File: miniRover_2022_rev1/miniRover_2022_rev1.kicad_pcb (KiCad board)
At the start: 2 copper layers, 11 parts, among them J1 XT60-M, U1 OKI, U2 DRV8871-Breakout-PCB, U3 DRV8871-Breakout-PCB, U4 DRV8871-Breakout-PCB, U5 DRV8871-Breakout-PCB, U6 DRV8871-Breakout-PCB, U7 DRV8871-Breakout-PCB

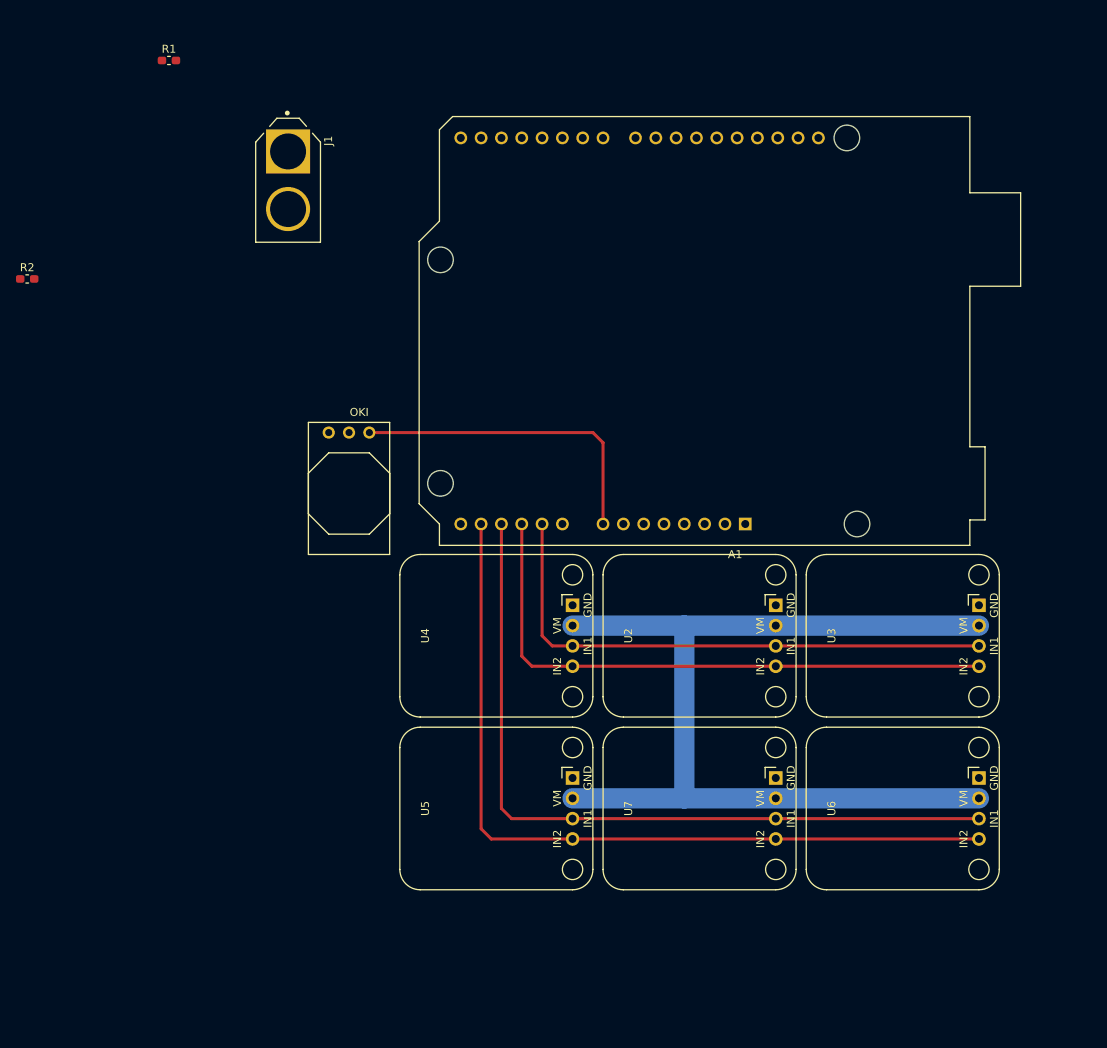
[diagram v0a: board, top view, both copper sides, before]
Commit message: gnd planes added
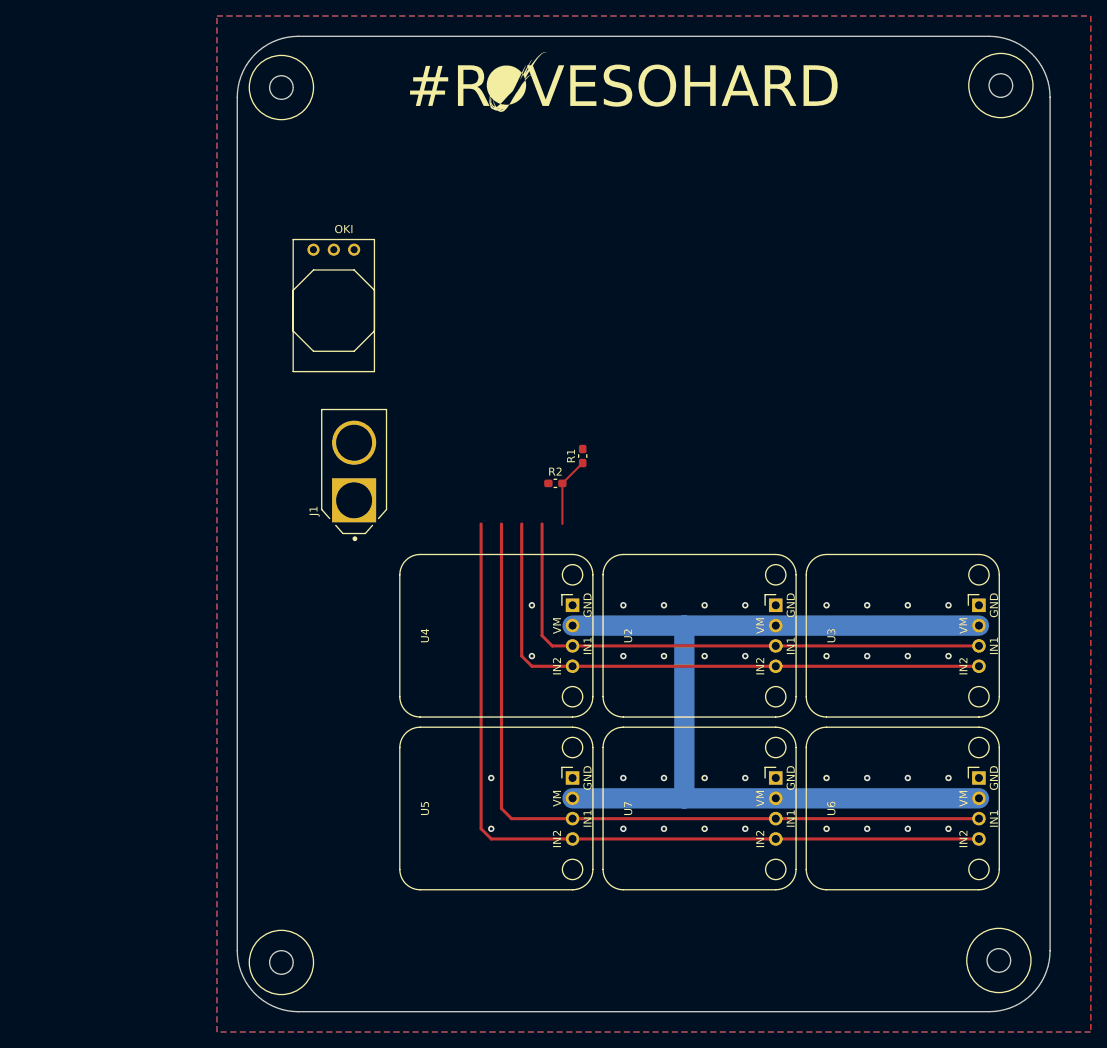
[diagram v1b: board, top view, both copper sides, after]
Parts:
- removed A1: Arduino_UNO_R3, Module:Arduino_UNO_R3_WithMountingHoles
- added G***: LOGO, MRDT_Silkscreens:0_MRDT_Logo_7.5mm, F.Cu at (149.2, 21.0)
- added REF**: 4_40_Hole, MRDT_Drill_Holes:4_40_Hole_Corner, F.Cu at (205.5, 126.8)
- added REF**: 4_40_Hole, MRDT_Drill_Holes:4_40_Hole_Corner, F.Cu at (123.8, 127.0)
- added REF**: 4_40_Hole, MRDT_Drill_Holes:4_40_Hole_Corner, F.Cu at (123.8, 25.6)
- added REF**: 4_40_Hole, MRDT_Drill_Holes:4_40_Hole_Corner, F.Cu at (205.7, 25.4)
- moved R1 71.6 mm to (157.5, 67.7), turned to 90 degrees
- moved R2 70.8 mm to (154.1, 71.1)
- moved J1 37.3 mm to (128.9, 69.6), turned to 90 degrees
- moved U1 22.9 mm to (123.8, 41.9)
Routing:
- net +5V: track 39.9 -> 0.00 mm
- net Net-(A1-Pad9): track 0.00 -> 8.67 mm
- net GND: vias 0 -> 36
- added copper zone on B.Cu, net GND
- added copper zone on F.Cu, net GND
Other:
- board outline added: 101.6 x 121.9 mm
- board text added: "#R VESOHARD"

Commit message: rev1 finished, will be reviewing over the following days
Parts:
- added A1: Arduino_UNO_R3, Module:Arduino_UNO_R3_WithMountingHoles, B.Cu at (174.0, 29.2)
- added G***: LOGO, MRDT_Silkscreens:0_MRDT_Logo_7.5mm, B.Cu at (176.5, 21.0)
- added G***: LOGO, miniRover2022:maxsignature, F.Cu at (125.7, 115.6)
- moved R2 51.8 mm to (127.4, 26.7)
- moved R1 46.1 mm to (130.8, 30.1), turned to 270 degrees
- moved J1 27.9 mm to (120.7, 96.3)
- moved U1 4.62 mm to (119.4, 40.6)
- moved U2 3.81 mm to (181.6, 90.2)
- moved U3 3.81 mm to (207.0, 90.2)
- moved U4 3.81 mm to (156.2, 90.2)
- moved U5 3.81 mm to (156.2, 111.8)
- moved U6 3.81 mm to (207.0, 111.8)
- moved U7 3.81 mm to (181.6, 111.8)
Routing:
- net +12V: track 123.2 -> 186.1 mm
- net +5V: track 0.00 -> 42.4 mm
- net Net-(A1-Pad9): track 8.67 -> 27.7 mm
- net /motorControllers/RIN1: track 95.8 -> 94.5 mm
- net /motorControllers/RIN2: track 100.9 -> 102.1 mm
- net /motorControllers/LIN2: track 74.2 -> 72.9 mm
- net GND: vias 36 -> 58
- added copper zone on B.Cu, net +12V
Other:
- outline, holes or cut-outs redrawn
- board text added: "LEFT MOTORS"
- board text added: "Mini Rover Power Board Mars Rover Design Team Missouri S&T, 2022 Maxwell Ryan"
- board text added: "RIGHT MOTORS"

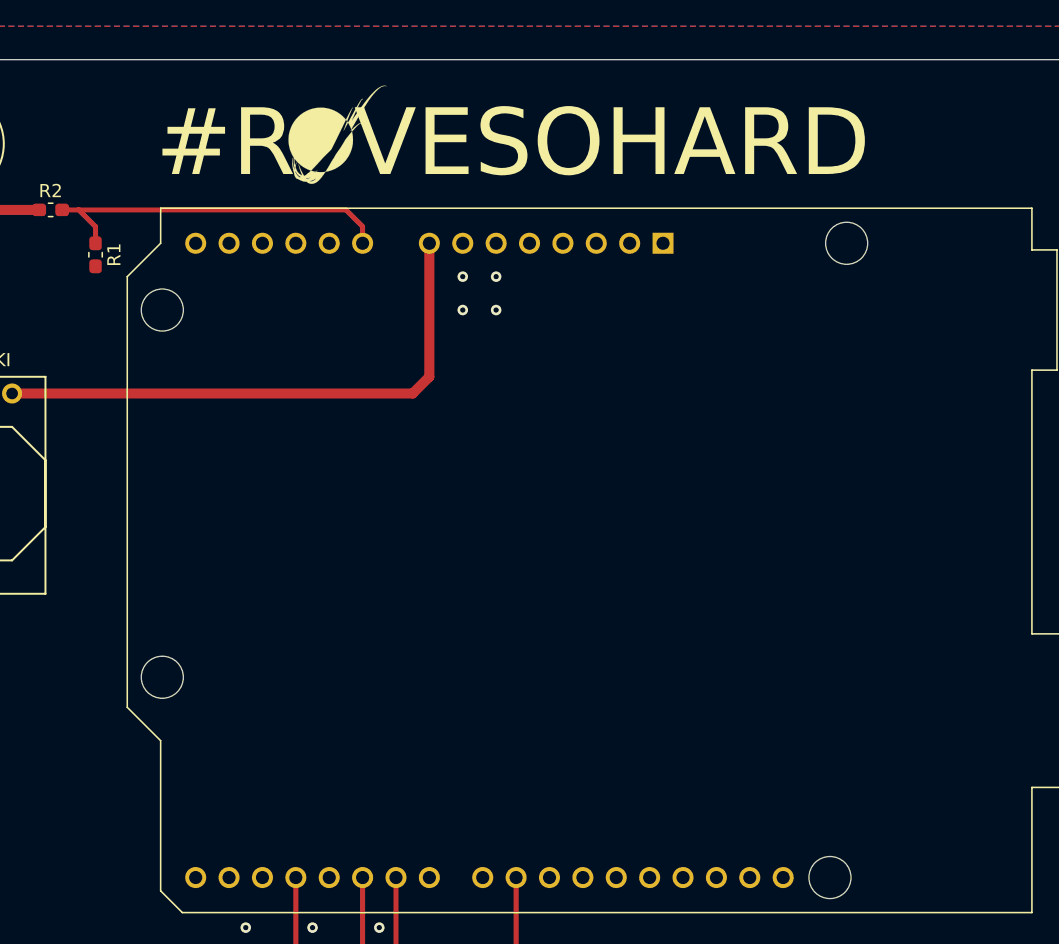
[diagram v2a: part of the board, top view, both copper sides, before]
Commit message: fixed arduino footprint issue
created proper netlist
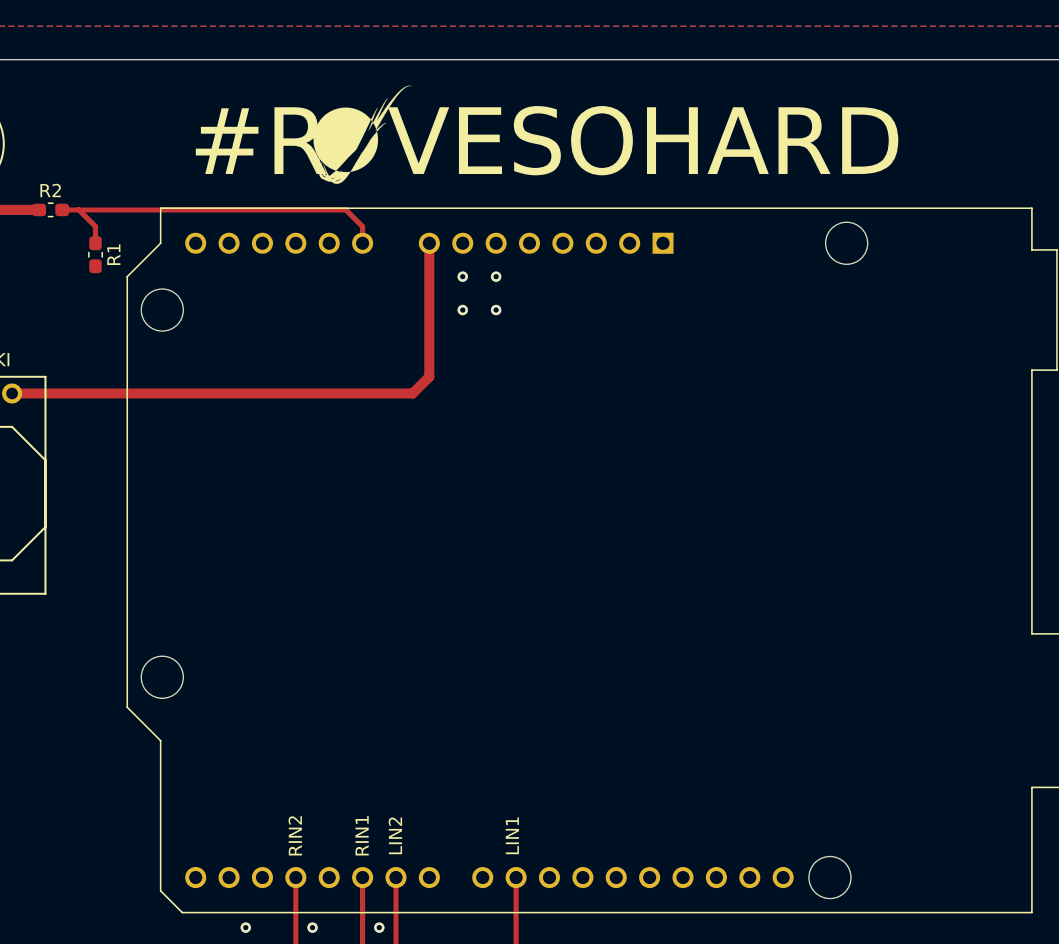
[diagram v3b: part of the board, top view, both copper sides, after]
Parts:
- moved G*** 2.54 mm to (179.1, 21.0)
- moved G*** 1.91 mm to (151.1, 21.0)
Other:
- board text added: "LIN1"
- board text added: "LIN2"
- board text added: "RIN1"
- board text added: "RIN2"
